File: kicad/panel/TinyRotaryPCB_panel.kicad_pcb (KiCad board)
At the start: 2 copper layers, 48 x 40 mm, 80 parts, among them J1 Conn_01x05_Pin, SW1 RotaryEncoder_Switch

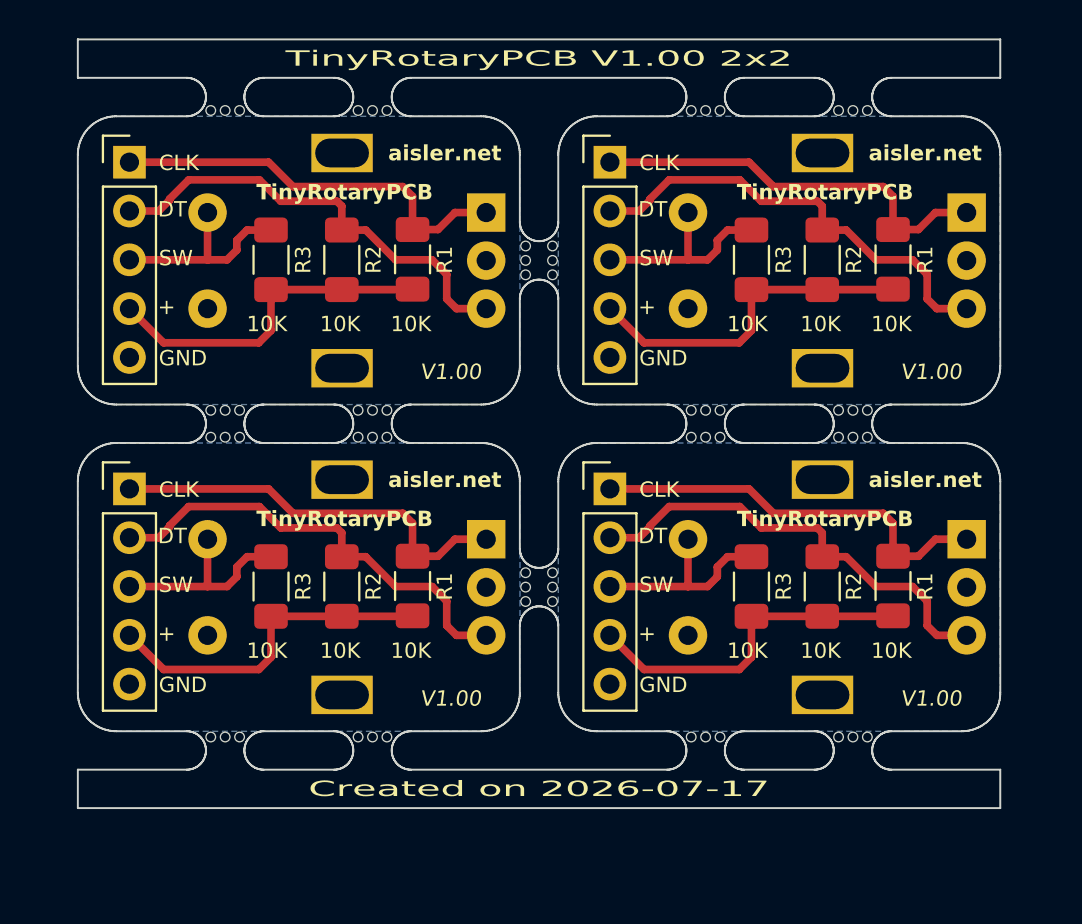
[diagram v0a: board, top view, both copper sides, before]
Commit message: Update KiCad project, horizontal pin header
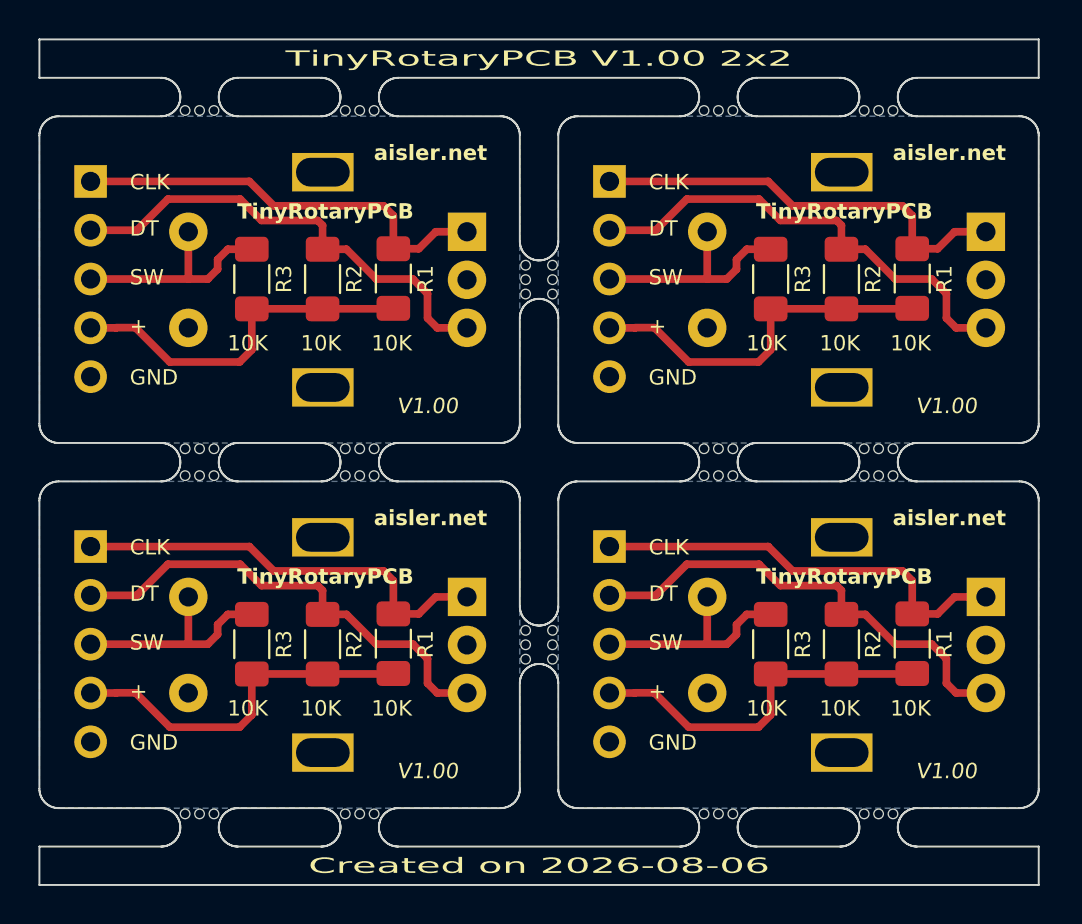
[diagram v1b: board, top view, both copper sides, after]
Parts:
- removed the J1 at (152.2, 26.4)
- removed the J1 at (127.2, 43.4)
- removed the J1 at (152.2, 43.4)
- removed the J1 at (127.2, 26.4)
- removed the R1 at (141.9, 48.4)
- removed the R1 at (166.9, 31.4)
- removed the R1 at (141.9, 31.4)
- removed the R1 at (166.9, 48.4)
- removed the R2 at (138.2, 31.5)
- removed the R2 at (163.2, 48.5)
- removed the R2 at (163.2, 31.5)
- removed the R2 at (138.2, 48.5)
- removed the R3 at (134.6, 48.5)
- removed the R3 at (159.6, 48.5)
- removed the R3 at (134.6, 31.5)
- removed the R3 at (159.6, 31.5)
- removed the SW1 at (163.2, 31.5)
- removed the SW1 at (138.3, 48.5)
- removed the SW1 at (138.3, 31.5)
- removed the SW1 at (163.2, 48.5)
- added J1: Conn_01x05_Pin, PinHeader_1x05_P2.54mm_H_W_S:PinHeader_1x05_P2.54mm_Horizontal_Without_Silkscreen, B.Cu at (152.2, 46.4)
- added J1: Conn_01x05_Pin, PinHeader_1x05_P2.54mm_H_W_S:PinHeader_1x05_P2.54mm_Horizontal_Without_Silkscreen, B.Cu at (152.2, 27.4)
- added J1: Conn_01x05_Pin, PinHeader_1x05_P2.54mm_H_W_S:PinHeader_1x05_P2.54mm_Horizontal_Without_Silkscreen, B.Cu at (125.2, 46.4)
- added J1: Conn_01x05_Pin, PinHeader_1x05_P2.54mm_H_W_S:PinHeader_1x05_P2.54mm_Horizontal_Without_Silkscreen, B.Cu at (125.2, 27.4)
- added R1: 10K, Resistor_SMD:R_1206_3216Metric_Pad1.30x1.75mm_HandSolder, F.Cu at (140.9, 32.4)
- added R1: 10K, Resistor_SMD:R_1206_3216Metric_Pad1.30x1.75mm_HandSolder, F.Cu at (140.9, 51.4)
- added R1: 10K, Resistor_SMD:R_1206_3216Metric_Pad1.30x1.75mm_HandSolder, F.Cu at (167.9, 32.4)
- added R1: 10K, Resistor_SMD:R_1206_3216Metric_Pad1.30x1.75mm_HandSolder, F.Cu at (167.9, 51.4)
- added R2: 10K, Resistor_SMD:R_1206_3216Metric_Pad1.30x1.75mm_HandSolder, F.Cu at (137.2, 32.5)
- added R2: 10K, Resistor_SMD:R_1206_3216Metric_Pad1.30x1.75mm_HandSolder, F.Cu at (164.2, 51.5)
- added R2: 10K, Resistor_SMD:R_1206_3216Metric_Pad1.30x1.75mm_HandSolder, F.Cu at (137.2, 51.5)
- added R2: 10K, Resistor_SMD:R_1206_3216Metric_Pad1.30x1.75mm_HandSolder, F.Cu at (164.2, 32.5)
- added R3: 10K, Resistor_SMD:R_1206_3216Metric_Pad1.30x1.75mm_HandSolder, F.Cu at (160.6, 51.5)
- added R3: 10K, Resistor_SMD:R_1206_3216Metric_Pad1.30x1.75mm_HandSolder, F.Cu at (133.6, 32.5)
- added R3: 10K, Resistor_SMD:R_1206_3216Metric_Pad1.30x1.75mm_HandSolder, F.Cu at (160.6, 32.5)
- added R3: 10K, Resistor_SMD:R_1206_3216Metric_Pad1.30x1.75mm_HandSolder, F.Cu at (133.6, 51.5)
- added SW1: RotaryEncoder_Switch, RotaryEncoders_PEC11R:RotaryEncoder_Bourns_Vertical_PEC11R-4xxxF-Sxxxx, B.Cu at (164.2, 51.5)
- added SW1: RotaryEncoder_Switch, RotaryEncoders_PEC11R:RotaryEncoder_Bourns_Vertical_PEC11R-4xxxF-Sxxxx, B.Cu at (137.2, 32.5)
- added SW1: RotaryEncoder_Switch, RotaryEncoders_PEC11R:RotaryEncoder_Bourns_Vertical_PEC11R-4xxxF-Sxxxx, B.Cu at (164.2, 32.5)
- added SW1: RotaryEncoder_Switch, RotaryEncoders_PEC11R:RotaryEncoder_Bourns_Vertical_PEC11R-4xxxF-Sxxxx, B.Cu at (137.2, 51.5)
- moved KiKit_MB_14_2 4.22 mm to (131.6, 60.3)
- moved KiKit_MB_14_3 4.22 mm to (130.8, 60.3)
- moved KiKit_MB_14_4 4.22 mm to (130.1, 60.3)
- moved KiKit_MB_20_2 4.22 mm to (166.9, 60.3)
- moved KiKit_MB_20_3 4.22 mm to (166.2, 60.3)
- moved KiKit_MB_20_4 4.22 mm to (165.4, 60.3)
- moved KiKit_MB_15_2 4.06 mm to (139.9, 60.3)
- moved KiKit_MB_15_3 4.06 mm to (139.2, 60.3)
- moved KiKit_MB_15_4 4.06 mm to (138.4, 60.3)
- moved KiKit_MB_19_2 4.06 mm to (158.6, 60.3)
- moved KiKit_MB_19_3 4.06 mm to (157.8, 60.3)
- moved KiKit_MB_19_4 4.06 mm to (157.1, 60.3)
- moved KiKit_MB_11_2 3.00 mm to (147.8, 50.8)
- moved KiKit_MB_11_3 3.00 mm to (147.8, 51.5)
- moved KiKit_MB_11_4 3.00 mm to (147.8, 52.2)
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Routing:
- net Board_1-VCC: track 17.8 -> 18.9 mm
- net Board_3-VCC: track 17.8 -> 18.9 mm
- net Board_0-VCC: track 17.8 -> 18.9 mm
- net Board_2-VCC: track 17.8 -> 18.9 mm
- net Board_3-/CLK: track 21.4 -> 22.4 mm
- net Board_1-/SW: track 10.8 -> 11.8 mm
- net Board_1-/CLK: track 21.4 -> 22.4 mm
- net Board_3-/SW: track 10.8 -> 11.8 mm
- net Board_2-/CLK: track 21.4 -> 22.4 mm
- net Board_0-/SW: track 10.8 -> 11.8 mm
- net Board_0-/CLK: track 21.4 -> 22.4 mm
- net Board_2-/SW: track 10.8 -> 11.8 mm
- net Board_1-/DT: track 23.5 -> 24.5 mm
- net Board_3-/DT: track 23.5 -> 24.5 mm
- net Board_0-/DT: track 23.5 -> 24.5 mm
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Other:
- board size 48 x 40 mm -> 52 x 44 mm
- board text added: "Created on 2026-08-06"
- board text removed: "Created on 2026-07-17"
